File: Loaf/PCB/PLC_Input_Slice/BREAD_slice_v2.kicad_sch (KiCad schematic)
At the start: 35 parts, among them J1 10018783-10200TLF, J2 Barrel_Jack, J3 DB25_Socket, U1 MCP4922-EP, U2 MCP4922-EP, U3 MCP4922-EP, U4 MCP4922-EP, U5 MCP3208, U6 MCP2561-E-P, U7 MCP2515-xSO, Y1 16MHZ Crystal

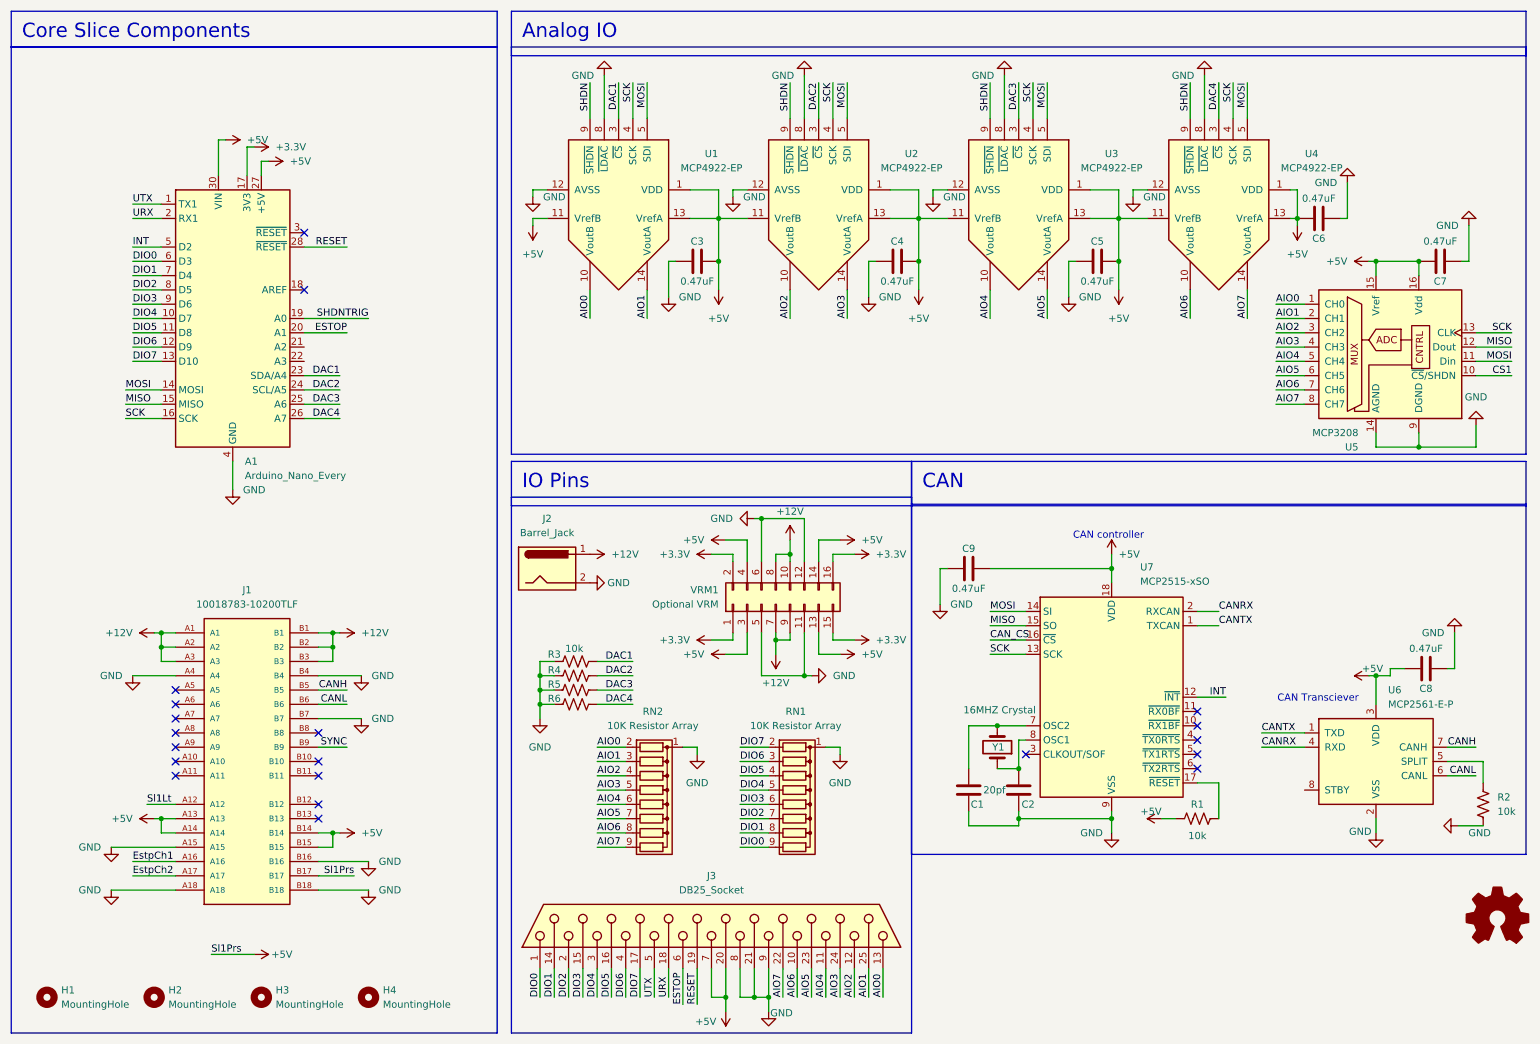
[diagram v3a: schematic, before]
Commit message: Fixed the I/O PCB because the routing was noisy
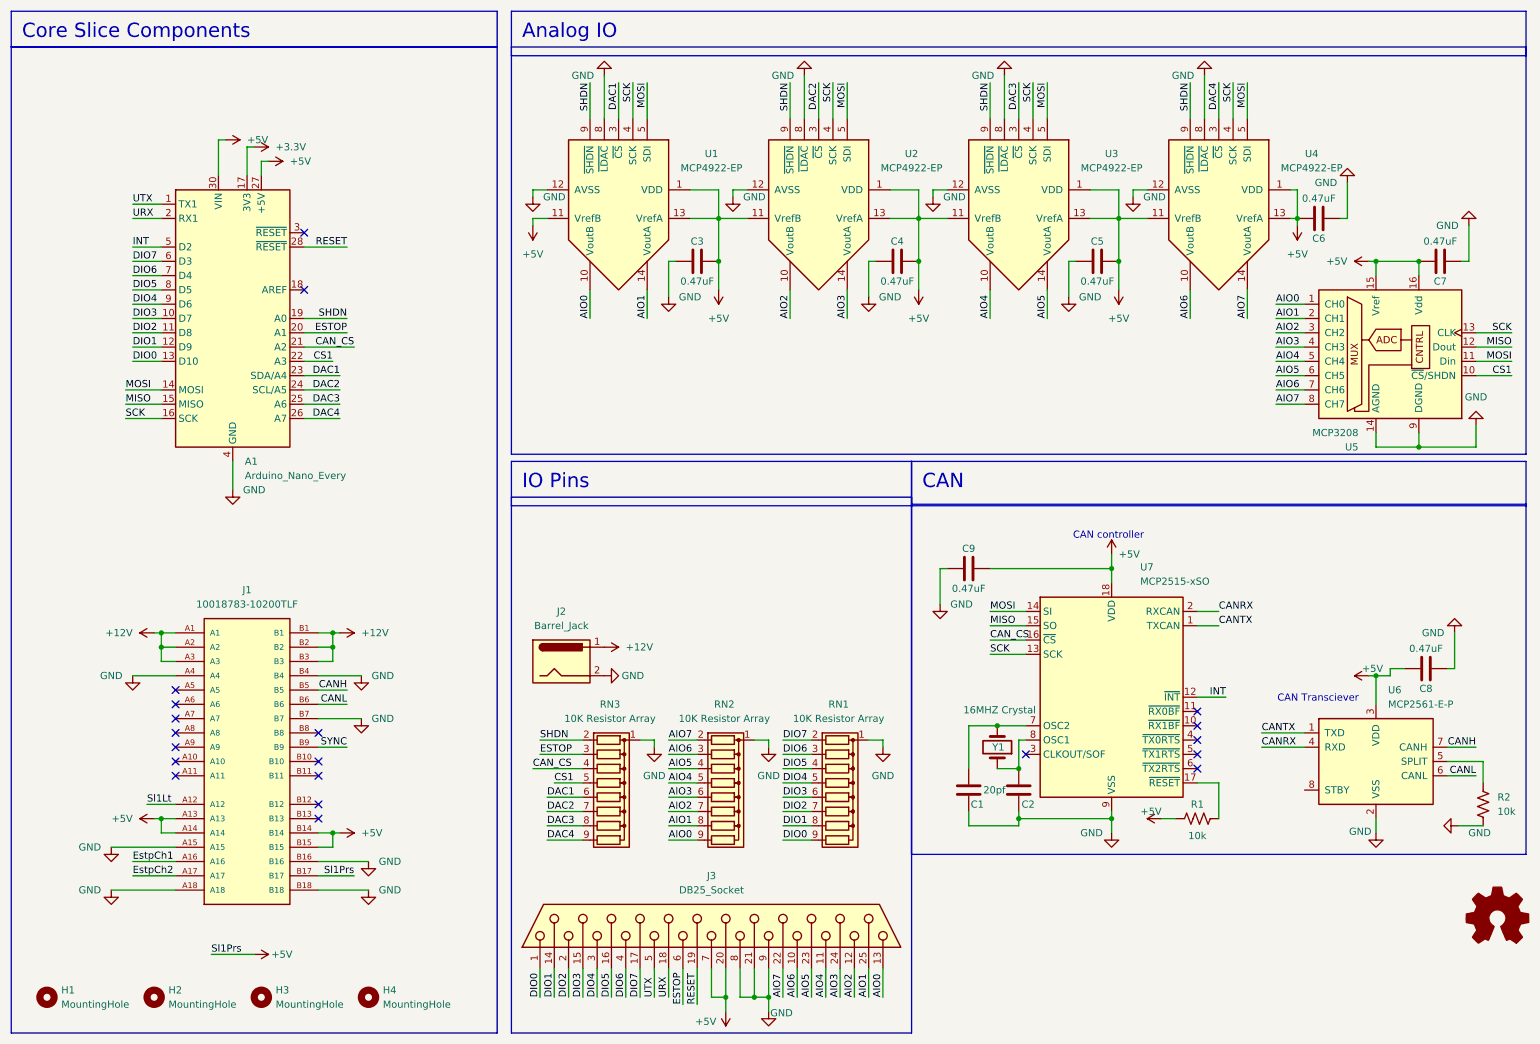
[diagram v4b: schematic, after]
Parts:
- removed R3, R4, R5, R6: 10k, R_Axial_DIN0207_L6.3mm_D2.5mm_P10.16mm_Horizontal, symbol Device:R_US
- removed VRM1: Optional VRM, PinSocket_2x08_P2.54mm_Vertical, symbol Connector_Generic:Conn_02x08_Odd_Even
- added RN3: 10K Resistor Array, Resistor_THT:R_Array_SIP9, symbol Device:R_Network08
- J2: footprint Connector_BarrelJack:BarrelJack_SwitchcraftConxall_RAPC10U_Horizontal -> BarrelJack_CUI_PJ-063AH_Horizontal
- U1, U2, U3, U4: footprint Package_DIP:DIP-14_W10.16mm_LongPads -> DIP-14_W7.62mm
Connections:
- net SHDNTRIG is gone; now on net SHDN: A1.19 (A0)
- net AIO0: now also RN2.9 (R8); no longer RN2.2 (R1)
- net AIO1: now also RN2.8 (R7); no longer RN2.3 (R2)
- net AIO2: now also RN2.7 (R6); no longer RN2.4 (R3)
- net AIO3: now also RN2.6 (R5); no longer RN2.5 (R4)
- net AIO4: now also RN2.5 (R4); no longer RN2.6 (R5)
- net AIO5: now also RN2.4 (R3); no longer RN2.7 (R6)
- net AIO6: now also RN2.3 (R2); no longer RN2.8 (R7)
- net AIO7: now also RN2.2 (R1); no longer RN2.9 (R8)
- net CAN_CS: now also A1.21 (A2), RN3.4 (R3)
- net CS1: now also A1.22 (A3), RN3.5 (R4)
- net DAC1: now also RN3.6 (R5)
- net DAC2: now also RN3.7 (R6)
- net DAC3: now also RN3.8 (R7)
- net DAC4: now also RN3.9 (R8)
- net DIO0: now also A1.13 (D10); no longer A1.6 (D3)
- net DIO1: now also A1.12 (D9); no longer A1.7 (D4)
- net DIO2: now also A1.11 (D8); no longer A1.8 (D5)
- net DIO3: now also A1.10 (D7); no longer A1.9 (D6)
- net DIO4: now also A1.9 (D6); no longer A1.10 (D7)
- net DIO5: now also A1.8 (D5); no longer A1.11 (D8)
- net DIO6: now also A1.7 (D4); no longer A1.12 (D9)
- net DIO7: now also A1.6 (D3); no longer A1.13 (D10)
- net ESTOP: now also RN3.3 (R2)
- net GND: now also RN3.1 (common)
- net SHDN: now also RN3.2 (R1)
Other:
- moved on the sheet: J2, RN1, RN2

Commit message: Updated Daughter Board
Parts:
- U5: footprint Package_DIP:DIP-16_W7.62mm_LongPads -> DIP-16_W7.62mm
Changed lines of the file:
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@@
 			)
 		)
-		(property "Footprint" "Package_DIP:DIP-16_W7.62mm_LongPads"
+		(property "Footprint" "DIP-16_W7.62mm"
 			(at 261.62 71.12 0)
 			(hide yes)

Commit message: Updated PCB Schematics
Added correct capacitor values and one missing resistor on USB card
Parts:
- C3, C4, C5, C6, C7, C8, C9: value 0.47uF -> 0.1uF
- U5: footprint DIP-16_W7.62mm -> Package_DIP:DIP-16_W7.62mm_LongPads
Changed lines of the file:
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@@
 			)
 		)
-		(property "Value" "0.47uF"
+		(property "Value" "0.1uF"
 			(at 135.89 61.976 90)
 			(show_name no)
@@
 			)
 		)
-		(property "Value" "0.47uF"
+		(property "Value" "0.1uF"
 			(at 265.43 127.254 90)
 			(show_name no)
@@
 			)
 		)
-		(property "Value" "0.47uF"
+		(property "Value" "0.1uF"
 			(at 207.01 61.976 90)
 			(show_name no)
@@
 			)
 		)
-		(property "Value" "0.47uF"
+		(property "Value" "0.1uF"
 			(at 171.45 61.976 90)
 			(show_name no)
@@
 			)
 		)
-		(property "Value" "0.47uF"
+		(property "Value" "0.1uF"
 			(at 267.97 54.864 90)
 			(show_name no)
@@
 			)
 		)
-		(property "Value" "0.47uF"
+		(property "Value" "0.1uF"
 			(at 246.38 47.244 90)
 			(show_name no)
@@
 			)
 		)
-		(property "Footprint" "DIP-16_W7.62mm"
+		(property "Footprint" "Package_DIP:DIP-16_W7.62mm_LongPads"
 			(at 261.62 71.12 0)
 			(hide yes)
@@
 			)
 		)
-		(property "Value" "0.47uF"
+		(property "Value" "0.1uF"
 			(at 184.15 116.586 90)
 			(show_name no)

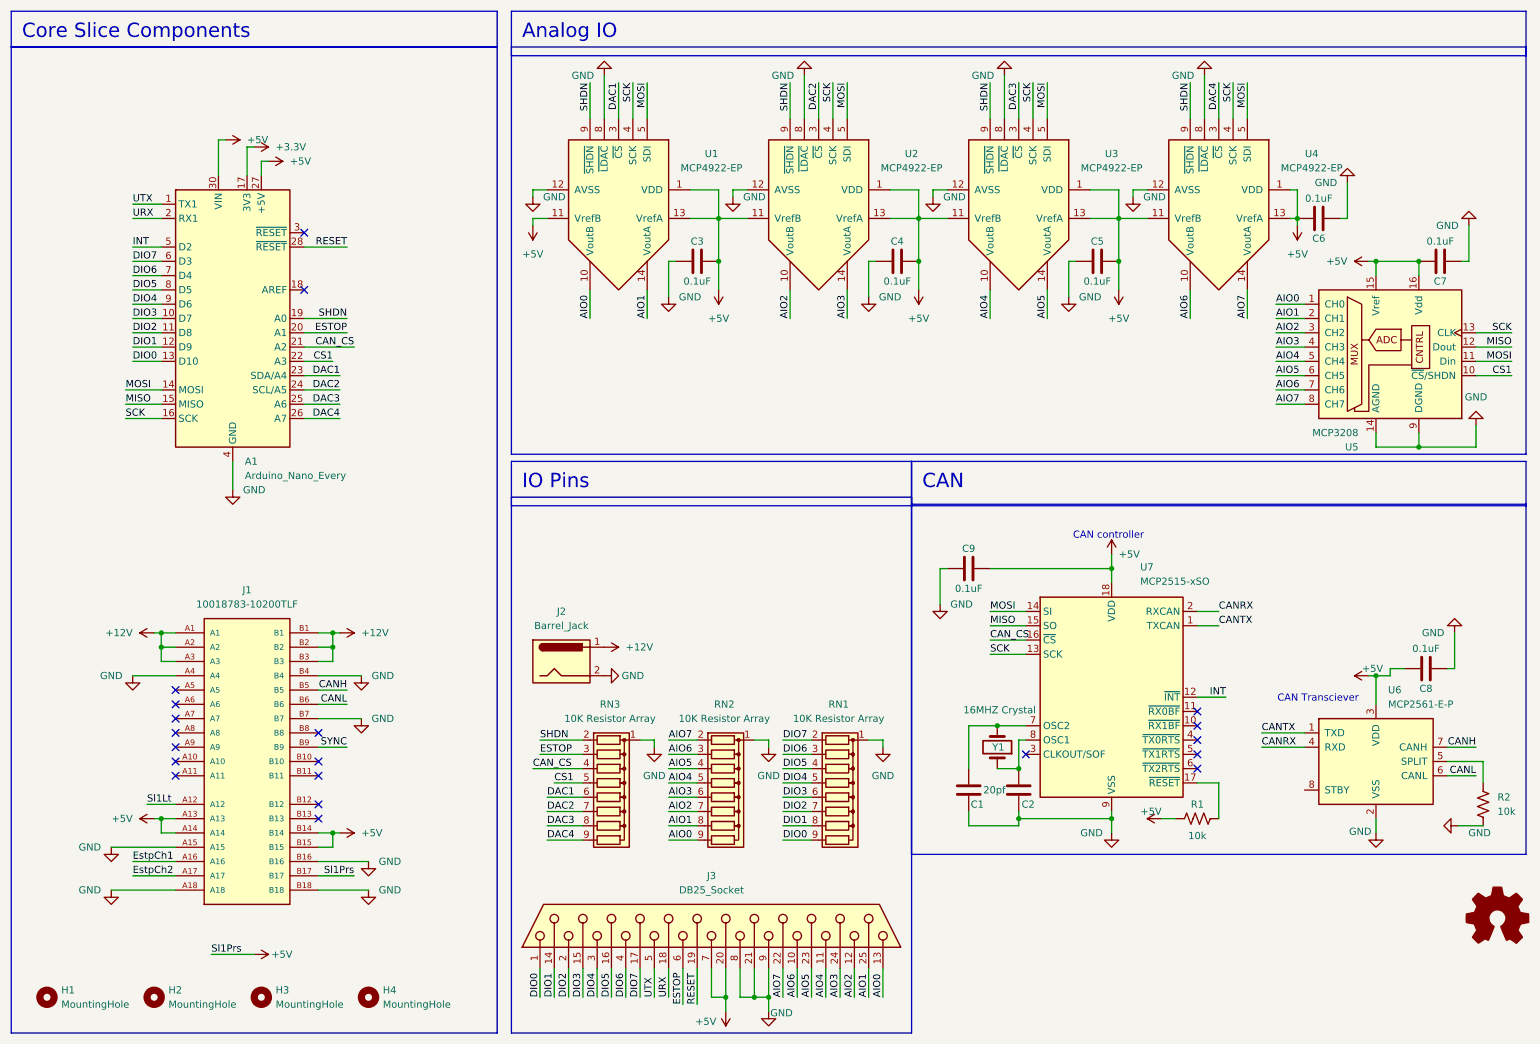
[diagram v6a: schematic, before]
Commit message: IO PCB redesign progress upload
Switching to pi pico for better performance and to keep UART interface
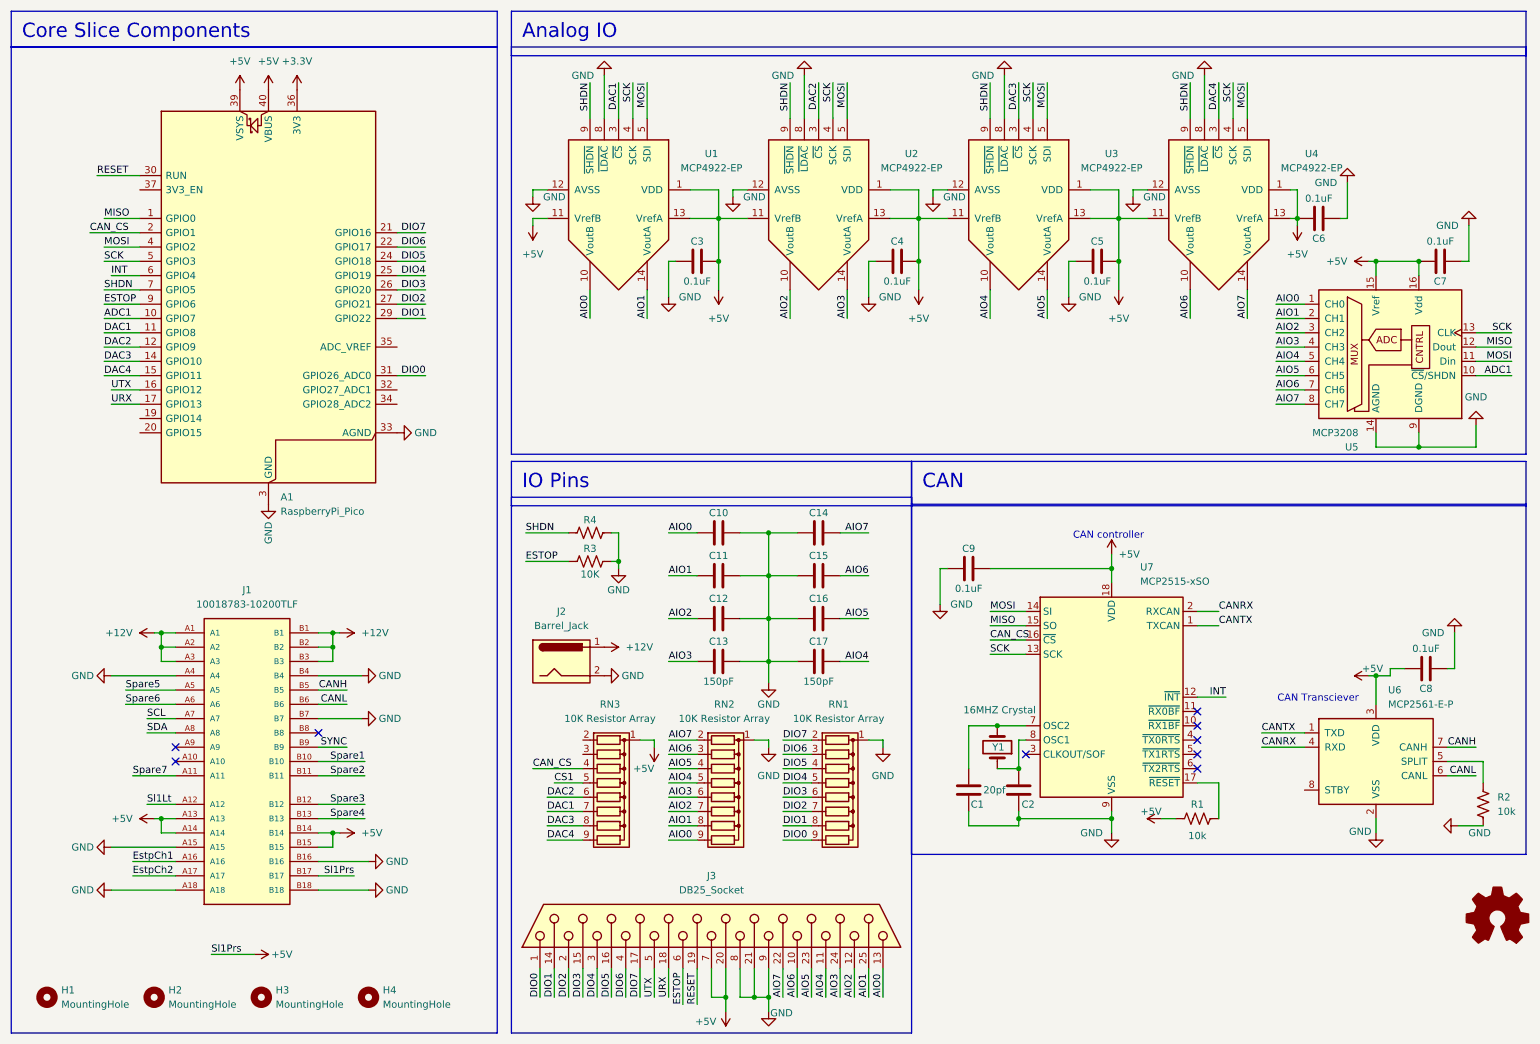
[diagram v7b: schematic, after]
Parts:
- removed A1: Arduino_Nano_Every, Module:Arduino_Nano, symbol MCU_Module:Arduino_Nano_Every
- added A1: RaspberryPi_Pico, Module:RaspberryPi_Pico_Common_Unspecified, symbol MCU_Module:RaspberryPi_Pico
- added C10, C11, C12, C14, C15, C16: 10pF, C_1206_3216Metric_Pad1.33x1.80mm_HandSolder, symbol Device:C
- added C13, C17: 150pF, C_1206_3216Metric_Pad1.33x1.80mm_HandSolder, symbol Device:C
- added R3, R4: 10K, R_Axial_DIN0207_L6.3mm_D2.5mm_P10.16mm_Horizontal, symbol Device:R_US
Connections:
- net +3.3V: now also A1.36 (3V3)
- net +5V: now also RN3.1 (common), A1.39 (VSYS), A1.40 (VBUS)
- net AIO0: now also C10.1
- net AIO1: now also C11.1
- net AIO2: now also C12.1
- net AIO3: now also C13.1
- net AIO4: now also C17.2
- net AIO5: now also C16.2
- net AIO6: now also C15.2
- net AIO7: now also C14.2
- net CAN_CS: now also A1.2 (GPIO1)
- net CS1: no longer U5.10 (~{CS}/SHDN)
- net DAC1: now also RN3.7 (R6), A1.11 (GPIO8); no longer RN3.6 (R5)
- net DAC2: now also RN3.6 (R5), A1.12 (GPIO9); no longer RN3.7 (R6)
- net DAC3: now also A1.14 (GPIO10)
- net DAC4: now also A1.15 (GPIO11)
- net DIO0: now also A1.31 (GPIO26_ADC0)
- net DIO1: now also A1.29 (GPIO22)
- net DIO2: now also A1.27 (GPIO21)
- net DIO3: now also A1.26 (GPIO20)
- net DIO4: now also A1.25 (GPIO19)
- net DIO5: now also A1.24 (GPIO18)
- net DIO6: now also A1.22 (GPIO17)
- net DIO7: now also A1.21 (GPIO16)
- net ESTOP: now also A1.9 (GPIO6), R3.1; no longer RN3.3 (R2)
- net GND: now also A1.13 (GND), A1.18 (GND), A1.23 (GND), A1.28 (GND), A1.3 (GND), A1.33 (AGND), A1.38 (GND), A1.8 (GND), C10.2, C11.2, C12.2, C13.2, C14.1, C15.1, C16.1, C17.1, R3.2, R4.2; no longer RN3.1 (common)
- net INT: now also A1.6 (GPIO4)
- net MISO: now also A1.1 (GPIO0)
- net MOSI: now also A1.4 (GPIO2)
- net RESET: now also A1.30 (RUN)
- net SCK: now also A1.5 (GPIO3)
- net SHDN: now also A1.7 (GPIO5), R4.1; no longer RN3.2 (R1)
- net URX: now also A1.17 (GPIO13)
- net UTX: now also A1.16 (GPIO12)
- net Spare7: now reaches J1.A11
- net Spare5: now reaches J1.A5
- net Spare6: now reaches J1.A6
- net SCL: now reaches J1.A7
- net SDA: now reaches J1.A8
- net Spare1: now reaches J1.B10
- net Spare2: now reaches J1.B11
- net Spare3: now reaches J1.B12
- net Spare4: now reaches J1.B13
- new net ADC1: A1.10 (GPIO7), U5.10 (~{CS}/SHDN)
- no-connect marks 20 -> 9

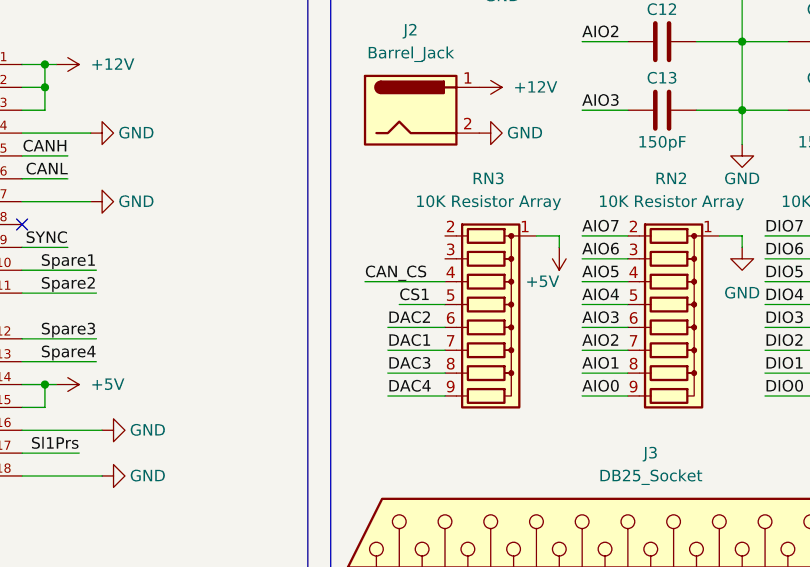
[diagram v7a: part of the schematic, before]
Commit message: Finished I/O Slice redesign with pico
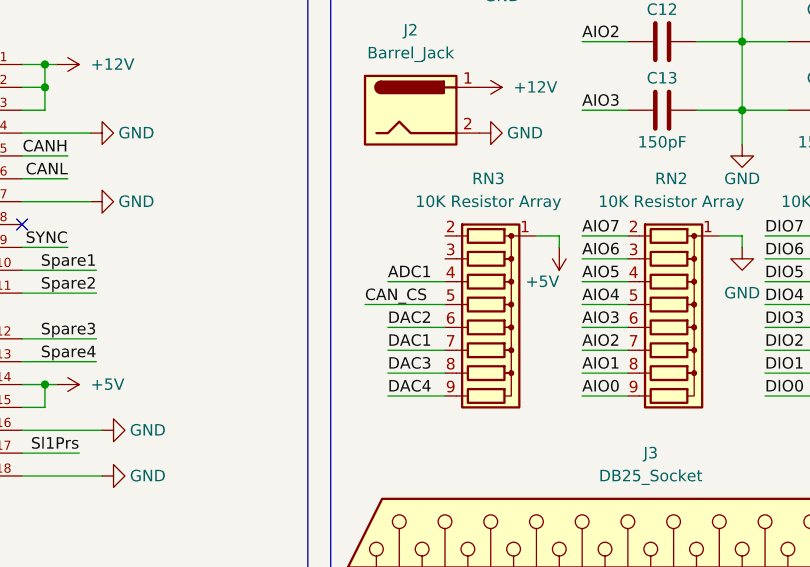
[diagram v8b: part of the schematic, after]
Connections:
- net CS1 is gone; now on net CAN_CS: RN3.5 (R4)
- net ADC1: now also RN3.4 (R3)
- net CAN_CS: no longer RN3.4 (R3)
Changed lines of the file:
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@@
 	(wire
 		(pts
-			(xy 115.57 151.13) (xy 110.49 151.13)
+			(xy 115.57 151.13) (xy 106.68 151.13)
 		)
 		(stroke
@@
 	(wire
 		(pts
+			(xy 109.22 148.59) (xy 115.57 148.59)
+		)
+		(stroke
+			(width 0)
+			(type default)
+		)
+	)
+	(wire
+		(pts
 			(xy 177.8 45.72) (xy 180.34 45.72)
 		)
@@
 	(wire
 		(pts
-			(xy 115.57 148.59) (xy 106.68 148.59)
-		)
-		(stroke
-			(width 0)
-			(type default)
-		)
-	)
-	(wire
-		(pts
 			(xy 30.48 58.42) (xy 36.83 58.42)
 		)
@@
 		)
 	)
-	(label "CS1"
-		(at 110.49 151.13 0)
-		(effects
-			(font
-				(size 1.27 1.27)
-			)
-			(justify left bottom)
-		)
-	)
 	(label "MOSI"
 		(at 233.68 26.67 270)
@@
 		)
 	)
+	(label "ADC1"
+		(at 109.22 148.59 0)
+		(effects
+			(font
+				(size 1.27 1.27)
+			)
+			(justify left bottom)
+		)
+	)
 	(label "DAC2"
 		(at 157.48 26.67 270)
@@
 	)
 	(label "CAN_CS"
-		(at 106.68 148.59 0)
+		(at 106.68 151.13 0)
 		(effects
 			(font
